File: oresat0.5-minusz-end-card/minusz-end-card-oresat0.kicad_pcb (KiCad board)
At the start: 4 copper layers, 99.8 x 94.6 mm, 28 parts, among them J2 Harwin M55-7101242R, J3 Harwin M55-7101242R, J4 Harwin M55-7101242R, J5 Harwin M55-7101242R

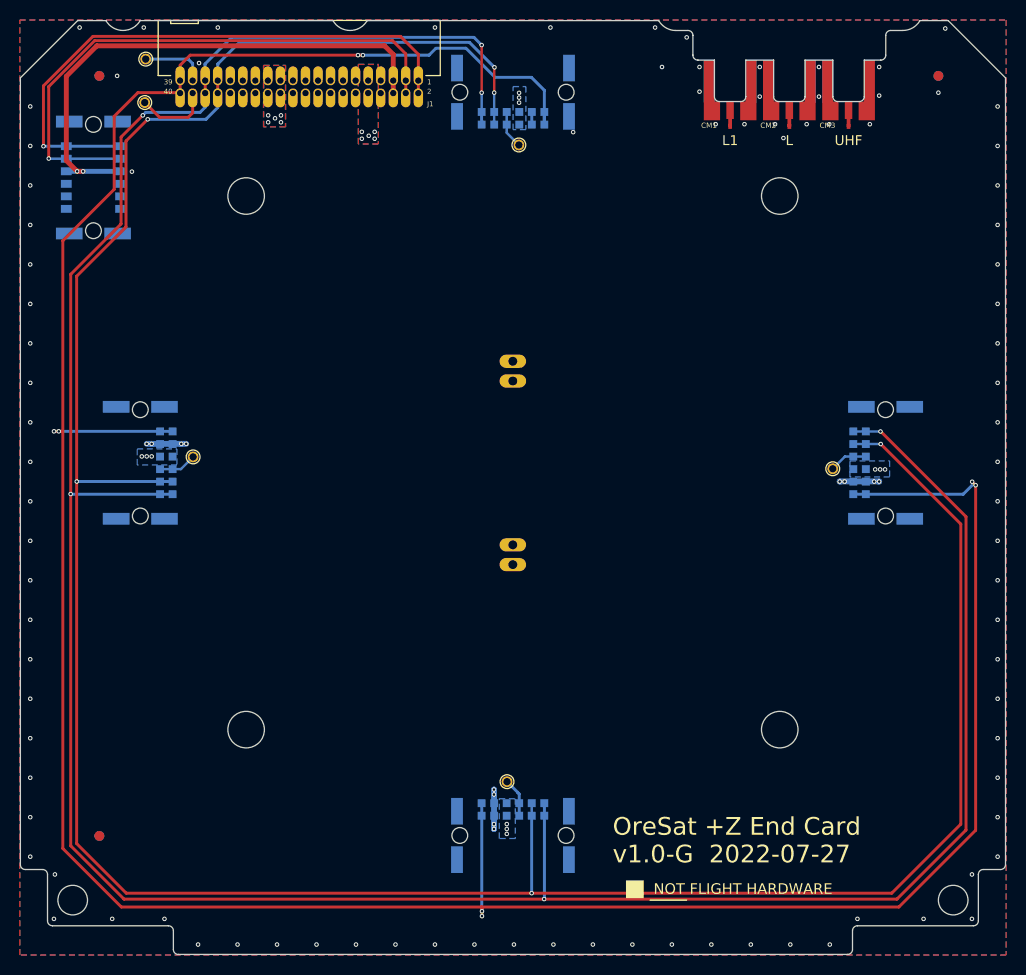
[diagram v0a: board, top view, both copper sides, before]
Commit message: Added new outline
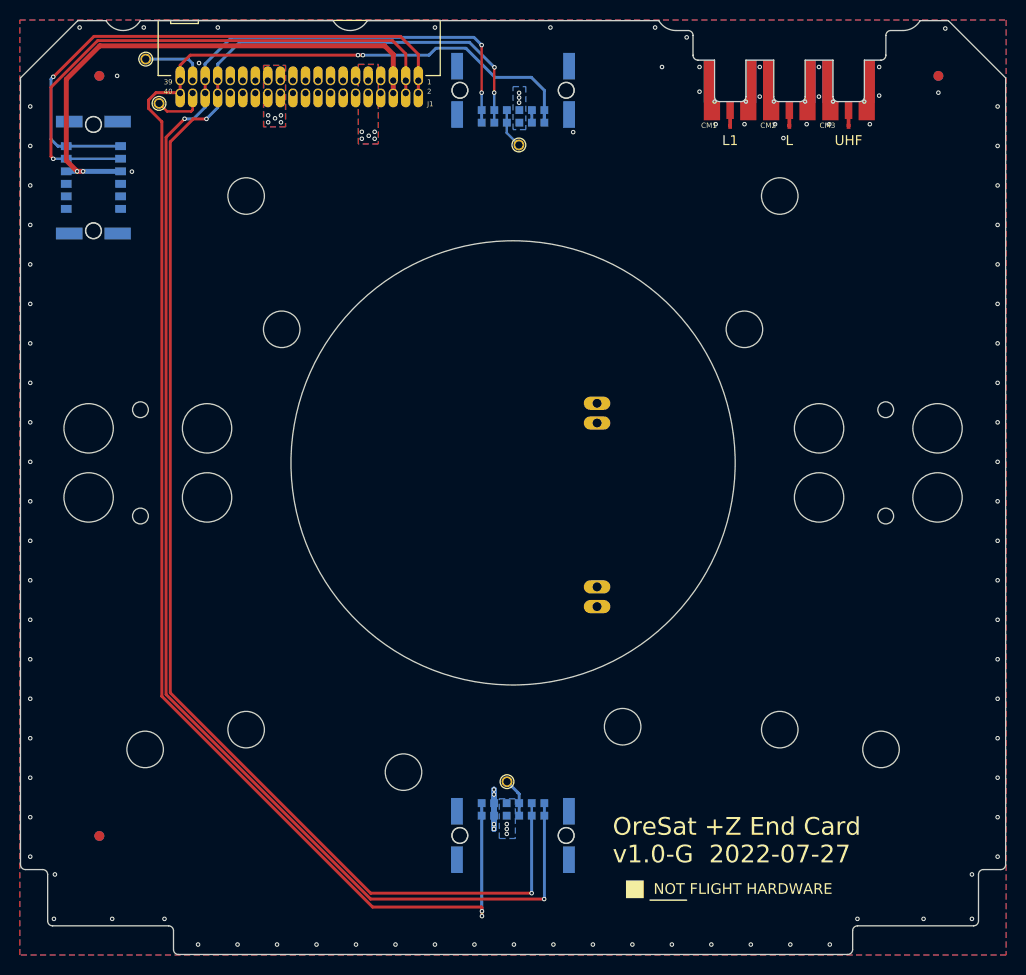
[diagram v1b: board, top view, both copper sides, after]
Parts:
- removed J2, J4: Harwin M55-7101242R, oresat-footprints:J-Harwin-M55-7101242R
- removed TP3, TP5: TEST-POINT-LARGE-SQUARE, plusz-end-card-with-turnstile:1X01
- moved R1 9.54 mm to (157.0, 106.8)
- moved TP2 1.45 mm to (112.6, 66.1)
- moved J5 0.19 mm to (148.5, 64.8)
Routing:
- net /CONNECTORS/~{SD}: track 303.4 -> 165.4 mm, vias 8 -> 4
- net /CONNECTORS/CAN1_L: track 288.1 -> 160.2 mm, vias 6 -> 4
- net /CONNECTORS/CAN1_H: track 282.2 -> 156.4 mm, vias 6 -> 4
- net GND: track 13.3 -> 5.27 mm, vias 106 -> 98
- net Net-(J4-Pad7): track 3.86 -> 0.00 mm
- net Net-(J2-Pad7): track 3.86 -> 0.00 mm
- net /CONNECTORS/C3-UART-RX: track 7.67 -> 5.51 mm
- net /CONNECTORS/MAG-SDA: track 58.7 -> 57.1 mm
- net /CONNECTORS/MAG-SCL: track 57.2 -> 56.6 mm
- net /CONNECTORS/VBUS: vias 17 -> 11
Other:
- outline, holes or cut-outs redrawn

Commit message: Updated -Z end card and replaced eagle imported libraries with kicad libraries
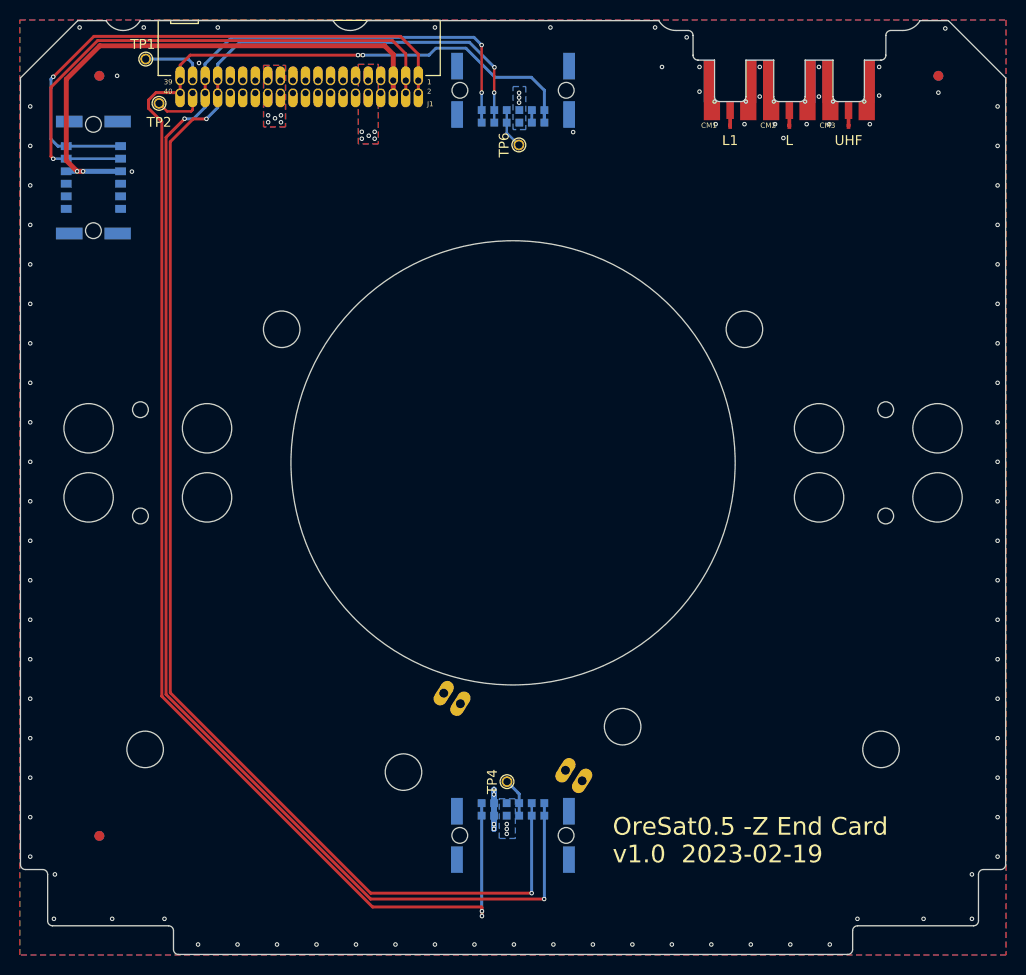
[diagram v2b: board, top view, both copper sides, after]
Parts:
- removed U$1: FLIGHMARKERNEW, plusz-end-card-with-turnstile:FLIGHTMARKER_NEW_BOARDS
- added HW5: M2-Press-Fit-Nut, oresat-misc:M2-Press-Fit-Nut, F.Cu at (172.0, 89.0)
- added HW6: M2-Press-Fit-Nut, oresat-misc:M2-Press-Fit-Nut, F.Cu at (125.1, 89.0)
- added REF**: MountingHole_5mm, MountingHole:MountingHole_5mm, F.Cu at (179.5, 99.0)
- added REF**: MountingHole_5mm, MountingHole:MountingHole_5mm, F.Cu at (117.5, 106.0)
- added REF**: MountingHole_5mm, MountingHole:MountingHole_5mm, F.Cu at (105.5, 99.0)
- added REF**: MountingHole_5mm, MountingHole:MountingHole_5mm, F.Cu at (191.5, 106.0)
- added REF**: MountingHole_5mm, MountingHole:MountingHole_5mm, F.Cu at (105.5, 106.0)
- added REF**: MountingHole_5mm, MountingHole:MountingHole_5mm, F.Cu at (191.5, 99.0)
- added REF**: MountingHole_5mm, MountingHole:MountingHole_5mm, F.Cu at (117.5, 99.0)
- added REF**: Hole-1.6mm-NPTH, oresat-misc:Hole-1.6mm-NPTH, F.Cu at (186.3, 107.9)
- added REF**: MountingHole_5mm, MountingHole:MountingHole_5mm, F.Cu at (179.5, 106.0)
- added REF**: Hole-1.6mm-NPTH, oresat-misc:Hole-1.6mm-NPTH, F.Cu at (186.3, 97.1)
- added REF**: Hole-1.6mm-NPTH, oresat-misc:Hole-1.6mm-NPTH, F.Cu at (110.8, 107.9)
- added REF**: Hole-1.6mm-NPTH, oresat-misc:Hole-1.6mm-NPTH, F.Cu at (110.8, 97.1)
- CF1: footprint plusz-end-card-with-turnstile:HARWIN-M55-60X1242R -> oresat-connectors:J-Harwin-M55-60X1242R
- CM1, CM2, CM3: footprint oresat-footprints:J-MOLEX-SMPM-073300-003X -> oresat-connectors:J-MOLEX-SMPM-073300-003X
- FID1: renamed from FIDUCIAL1; value FIDUCIAL-1.0X2.0 -> Fiducial; footprint plusz-end-card-with-turnstile:FIDUCIAL-1.0X2.0 -> Fiducial:Fiducial_1mm_Mask2mm
- FID2: renamed from FIDUCIAL2; value FIDUCIAL-1.0X2.0 -> Fiducial; footprint plusz-end-card-with-turnstile:FIDUCIAL-1.0X2.0 -> Fiducial:Fiducial_1mm_Mask2mm
- FID3: renamed from FIDUCIAL3; value FIDUCIAL-1.0X2.0 -> Fiducial; footprint plusz-end-card-with-turnstile:FIDUCIAL-1.0X2.0 -> Fiducial:Fiducial_1mm_Mask2mm
- FID4: renamed from FIDUCIAL4; value FIDUCIAL-1.0X2.0 -> Fiducial; footprint plusz-end-card-with-turnstile:FIDUCIAL-1.0X2.0 -> Fiducial:Fiducial_1mm_Mask2mm
- FID5: renamed from FIDUCIAL5; value FIDUCIAL-1.0X2.0 -> Fiducial; footprint plusz-end-card-with-turnstile:FIDUCIAL-1.0X2.0 -> Fiducial:Fiducial_1mm_Mask2mm
- FID6: renamed from FIDUCIAL6; value FIDUCIAL-1.0X2.0 -> Fiducial; footprint plusz-end-card-with-turnstile:FIDUCIAL-1.0X2.0 -> Fiducial:Fiducial_1mm_Mask2mm
- HW1, HW2, HW3, HW4: value MCMASTER-94100A150 -> M2-Press-Fit-Nut; footprint oresat-footprints:H-MCMASTER-94100A150 -> oresat-misc:M2-Press-Fit-Nut
- J1: value (none) -> J-SAMTEC-TFM-120-01-L-D-RA
- J3, J5: footprint oresat-footprints:J-Harwin-M55-7101242R -> oresat-connectors:J-Harwin-M55-7101242R
- R1: value 7.5 1W -> 7.5 1W; footprint oresat-footprints:R-PAC100-FOR-MELTWIRE -> oresat-passives:R-PAC100-FOR-MELTWIRE
- TP1, TP2, TP4, TP6: footprint plusz-end-card-with-turnstile:1X01 -> oresat-misc:TestPoint-MinTH
- moved HW3 60.5 mm to (137.4, 133.8)
- moved HW1 57.0 mm to (185.8, 131.5)
- moved R1 25.0 mm to (148.5, 130.3), turned to -122.35 degrees
- moved HW2 15.9 mm to (159.6, 129.2)
- moved HW4 10.4 mm to (111.2, 131.5)
- turned FID4 to -90 degrees
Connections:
- net /CONNECTORS/VBUS renamed VBUS
- net Net-(J3-Pad7) renamed /CONNECTORS/+X_AUX
- net Net-(J5-Pad7) renamed /CONNECTORS/-X_AUX
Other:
- outline, holes or cut-outs redrawn
- board text added: "OreSat0.5 -Z End Card"
- board text added: "v1.0 2023-02-19"
- board text removed: "OreSat +Z End Card"
- board text removed: "v1.0-G 2022-07-27"

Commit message: -Z end card design review changes, and added antenna feeds
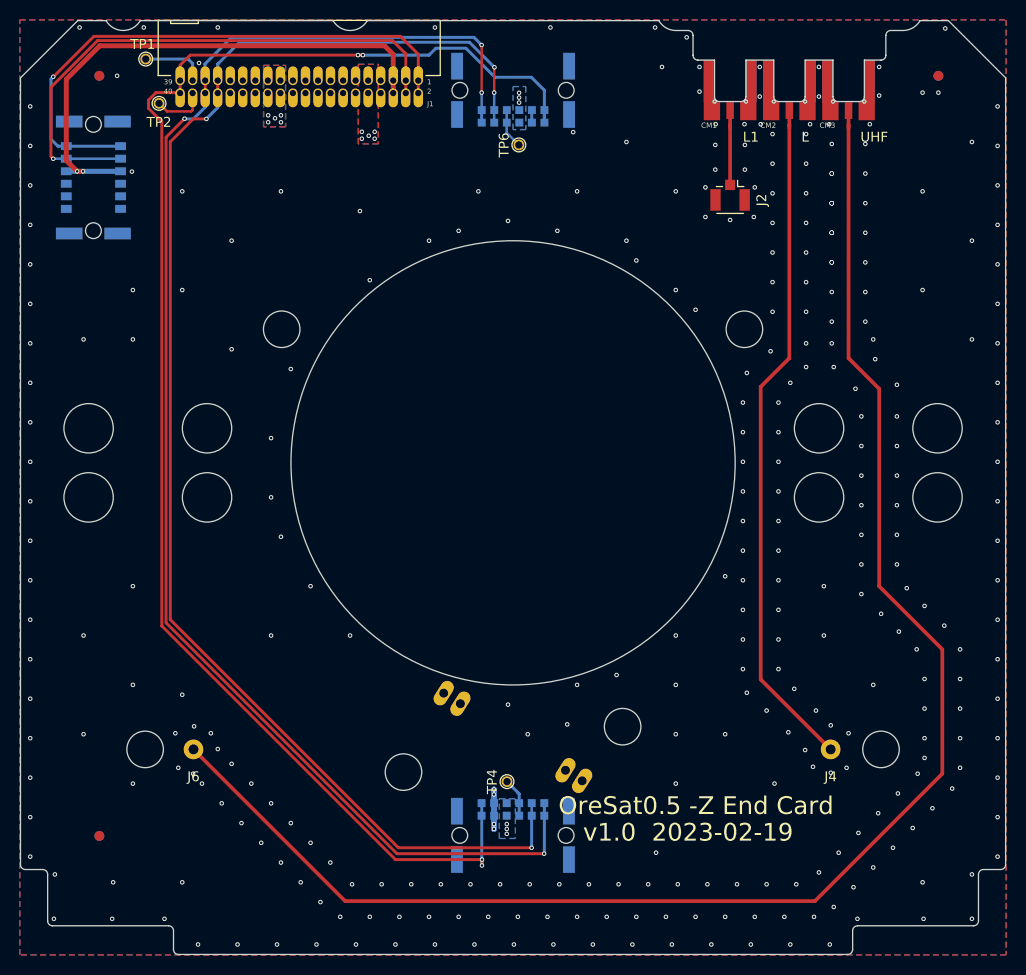
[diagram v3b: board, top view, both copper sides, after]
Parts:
- removed the REF** at (186.3, 107.9)
- removed the REF** at (186.3, 97.1)
- removed the REF** at (110.8, 107.9)
- removed the REF** at (110.8, 97.1)
- added J2: U.FL-R-SMT-1, Connector_Coaxial:U.FL_Hirose_U.FL-R-SMT-1_Vertical, F.Cu at (170.5, 75.4)
- added J4: L-Band Feed, Connector_Pin:Pin_D1.0mm_L10.0mm, F.Cu at (180.7, 131.5)
- added J6: UHF Feed, Connector_Pin:Pin_D1.0mm_L10.0mm, F.Cu at (116.1, 131.5)
- HW1, HW2, HW3, HW4, HW5, HW6: moved to B.Cu
- turned HW1 to 180 degrees
- turned HW2 to 180 degrees
- turned HW3 to 180 degrees
- turned HW4 to 180 degrees
- turned HW5 to 180 degrees
- turned HW6 to 180 degrees
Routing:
- net /UHF/UHF: track 0.00 -> 157.1 mm
- net /L BAND/LBAND: track 0.00 -> 67.3 mm
- net /CONNECTORS/~{SD}: track 165.4 -> 154.5 mm
- net /CONNECTORS/CAN1_H: track 156.4 -> 145.6 mm
- net /CONNECTORS/CAN1_L: track 160.2 -> 149.4 mm
- net /L1 BAND/L1BAND: track 0.00 -> 5.93 mm
- net GND: vias 98 -> 335

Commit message: Rounded out RF trace corners on -Z end card
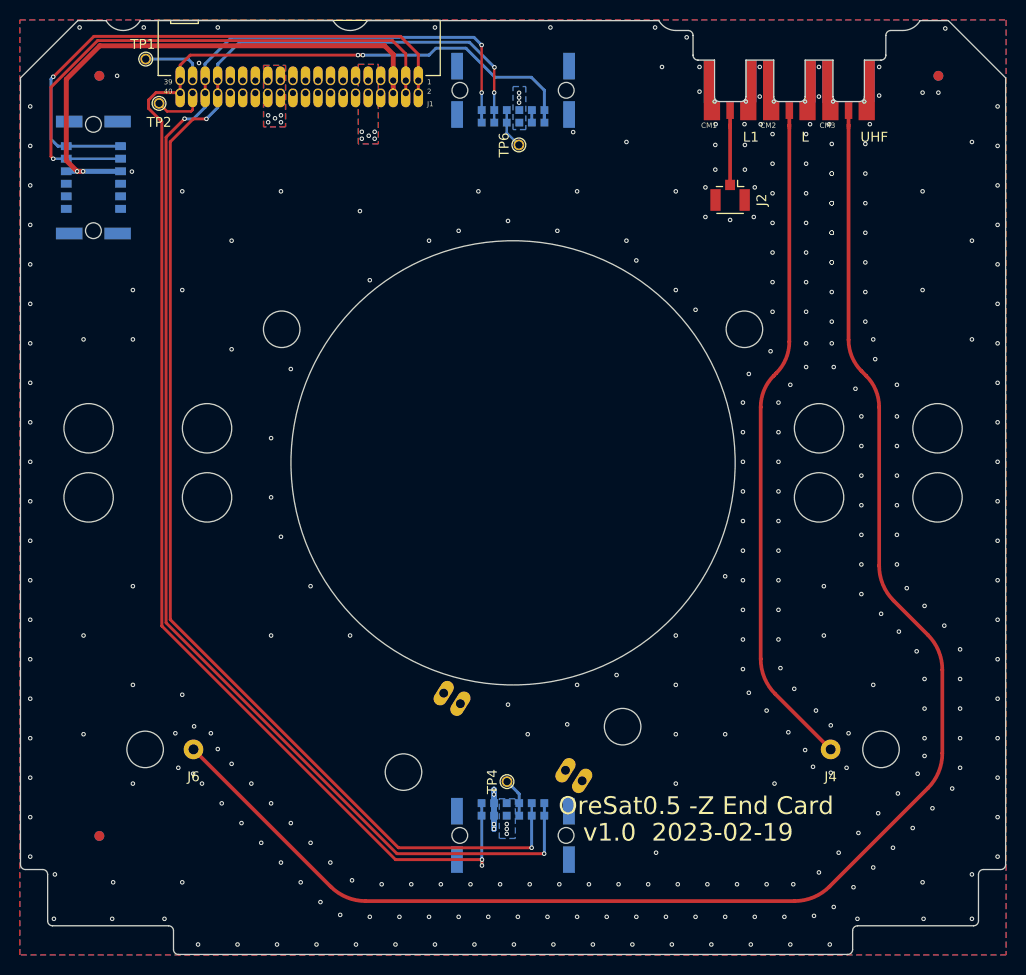
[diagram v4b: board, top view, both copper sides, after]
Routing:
- net /UHF/UHF: track 157.1 -> 155.5 mm
- net /L BAND/LBAND: track 67.3 -> 66.6 mm
